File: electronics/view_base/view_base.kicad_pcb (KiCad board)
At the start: 2 copper layers, 81.2 x 81.2 mm, 107 parts, among them J1 BLDC, J2 USB_C_Receptacle_USB2.0, J3 LCD, J4 A, J5 B, Q1 MMBT4403, Q2 UMH3N, U1 MT6701-CT, U2 T-Micro32_Plus, U3 CH340C, U4 HX711, U5 TMC6300, U6 AP2114HA-3.3, U7 SN74LV1T34DBV, U8 VEML7700, U9 TS1117BCW33_RPG

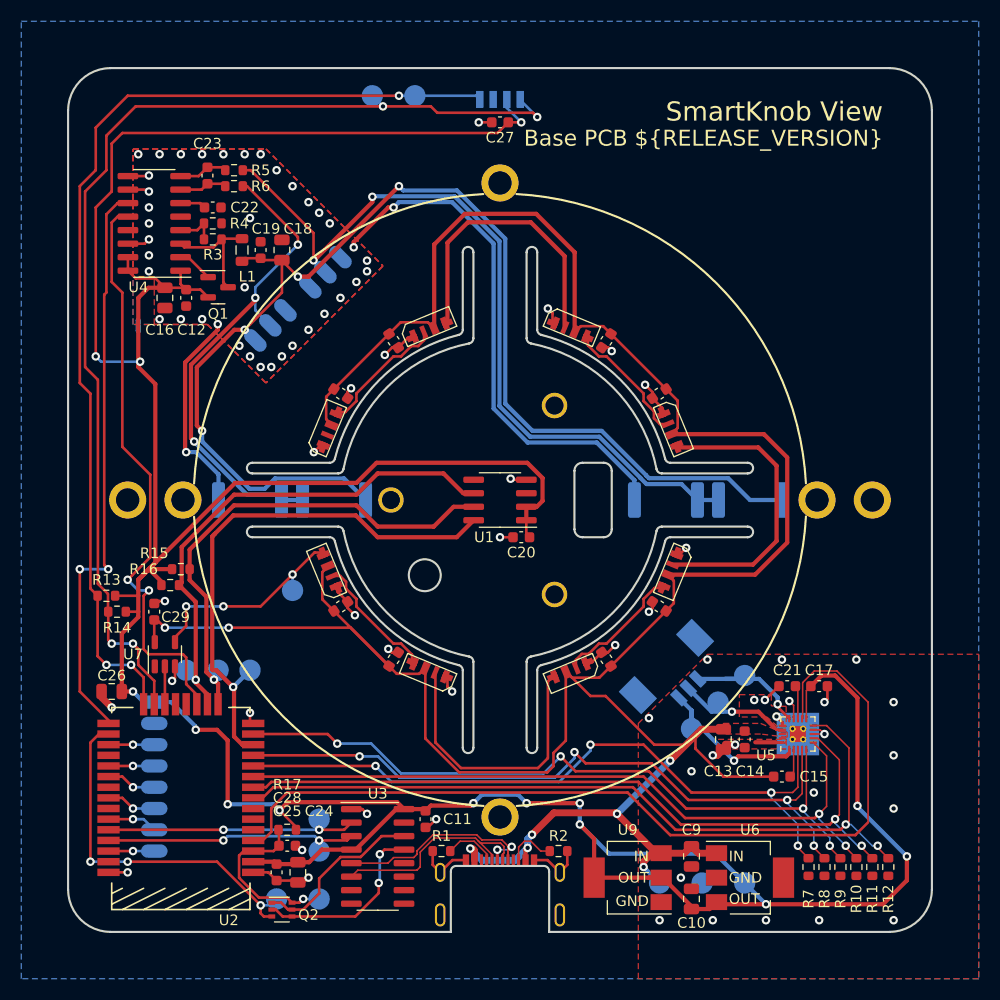
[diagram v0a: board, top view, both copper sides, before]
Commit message: Moved some holes around for another motor, cleaned up traces
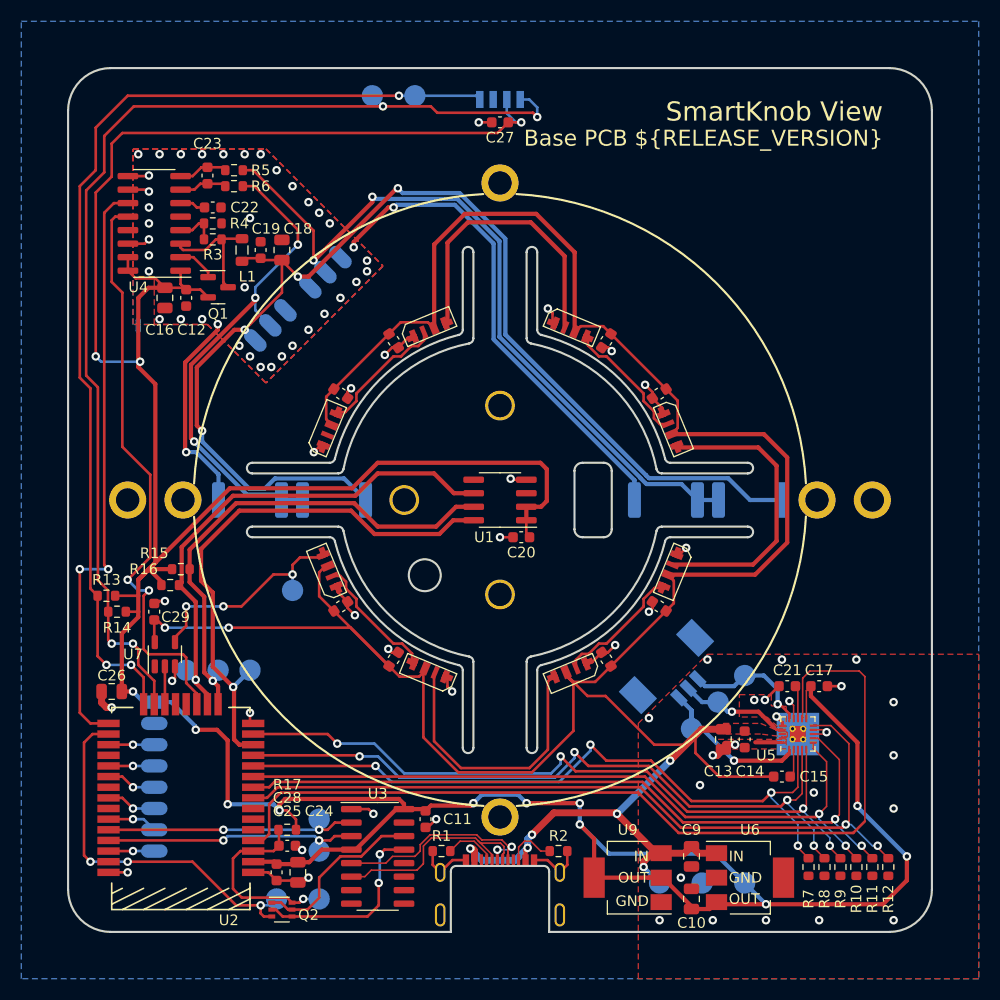
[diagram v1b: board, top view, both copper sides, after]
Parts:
- removed Z5: dummy_keepouts, view_custom:ViewKeepouts3d
- removed Z6, Z8: RotorScrew (BOM-only), BOM_Only:bom_only_no_pin
- moved H1 5.13 mm to (100.0, 108.9)
- moved H3 5.13 mm to (100.0, 91.1)
- moved H2 1.25 mm to (91.0, 100.0)
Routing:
- net Net-(J1-Pad3): track 18.4 -> 12.1 mm
- net GNDA: track 76.1 -> 72.0 mm
- net /STRAIN_E+: track 119.0 -> 115.0 mm
- net /STRAIN_S+: track 75.0 -> 71.3 mm
- net /MAG_CSN: track 54.0 -> 51.9 mm
- net /ESP32_EN: track 15.4 -> 17.0 mm
- net /STRAIN_SCK: track 54.5 -> 55.8 mm
- net /TMC_DIAG: track 85.9 -> 87.1 mm
- net Net-(J1-Pad2): track 13.6 -> 12.6 mm
- net +5V: track 256.1 -> 257.1 mm
- net GND: track 69.1 -> 70.1 mm
- net /ESP32_BOOT: track 34.9 -> 35.8 mm
- net /DTR: track 17.4 -> 18.1 mm
- net /TMC_UH: track 67.1 -> 67.8 mm
- net /TMC_WH: track 68.0 -> 68.7 mm
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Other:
- board text removed: "DATE: ${COMMIT_DATE_LONG} COMMIT: ${COMMIT_HASH}"
